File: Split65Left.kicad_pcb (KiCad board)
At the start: 2 copper layers, 176.6 x 97.8 mm, 77 parts, among them J1 Jack4, J2 OLED, SW1 SW_PUSH, SW10 SW_PUSH, SW11 SW_PUSH, SW12 SW_PUSH, SW13 SW_PUSH, SW14 SW_PUSH, SW15 SW_PUSH, SW16 SW_PUSH, SW17 SW_PUSH, SW18 SW_PUSH, SW19 SW_PUSH, SW2 SW_PUSH, SW20 SW_PUSH, SW21 SW_PUSH, SW22 SW_PUSH, SW23 SW_PUSH, SW24 SW_PUSH, SW25 SW_PUSH, SW26 SW_PUSH, SW27 SW_PUSH, SW28 SW_PUSH, SW29 SW_PUSH, SW3 SW_PUSH, SW30 SW_PUSH, SW31 SW_RST, SW4 SW_PUSH, SW5 SW_PUSH, SW6 SW_PUSH, SW7 SW_PUSH, SW8 SW_PUSH, SW9 SW_PUSH, U1 proton_c

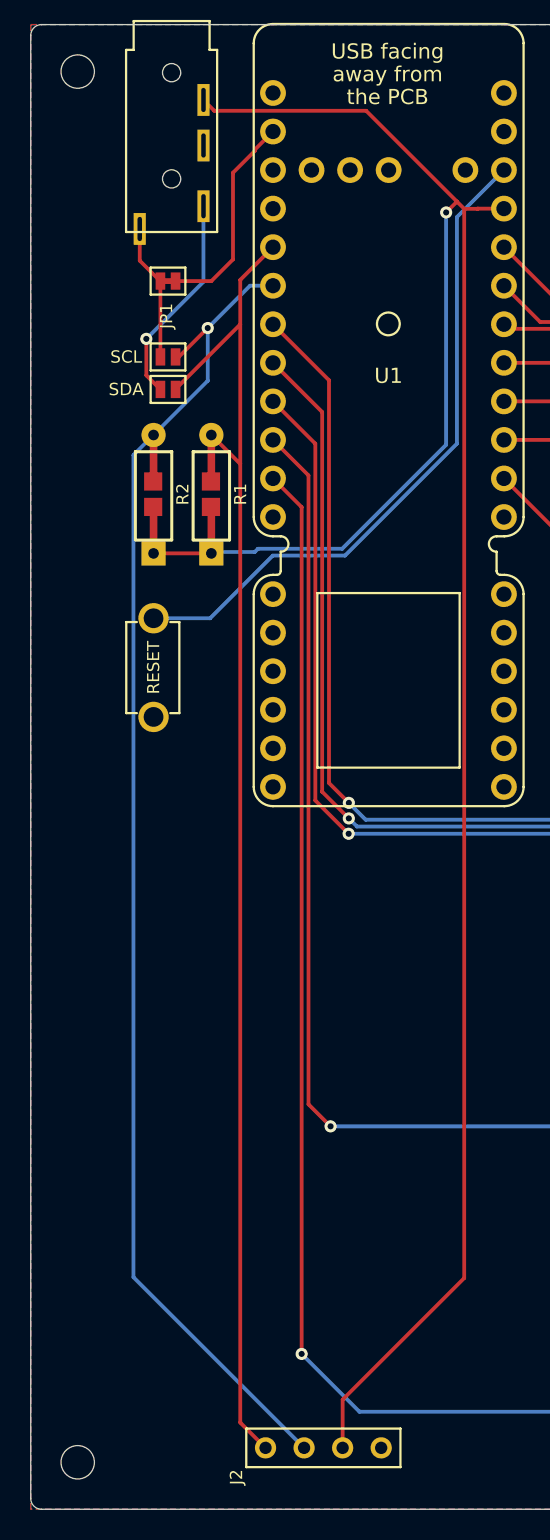
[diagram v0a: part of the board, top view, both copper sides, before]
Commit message: modified:   Split65Left-cache.lib 	modified:   Split65Left.kicad_pcb 	modified:   Split65Left.kicad_pcb-bak 	modified:   Split65Left.net 	modified:   Split65Left.sch 	modified:   Split65Left.sch-bak 	modified:   Split65Right-cache.lib 	modified:   Split65Right.kicad_pcb 	modified:   Split65Right.kicad_pcb-bak 	modified:   Split65Right.net 	modified:   Split65Right.sch 	modified:   Split65Right.sch-bak
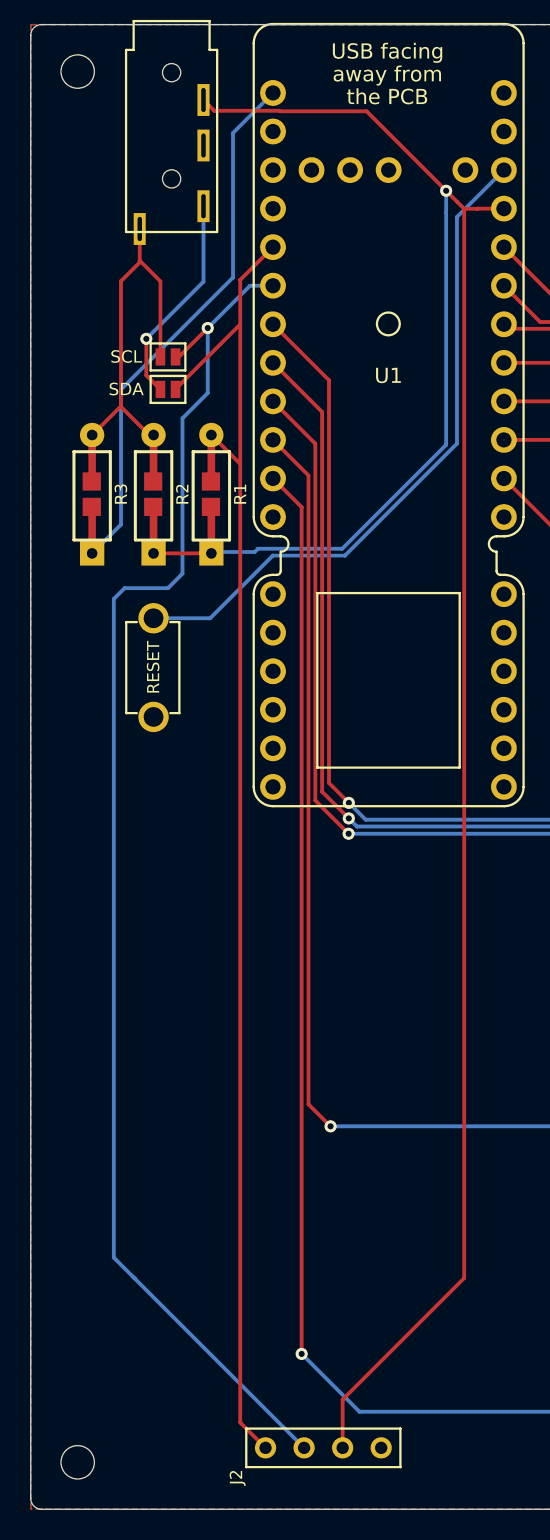
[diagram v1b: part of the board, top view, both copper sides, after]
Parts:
- removed JP1: Jumper, footprints:jumper_data
- added R3: 120, footprints:R_1608_axial, F.Cu at (62.6, 74.3)
- R1, R2: value R -> 5k
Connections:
- R2 pad 2: SCL -> Net-(J1-PadT)
- U1 pad A10: DATA -> Net-(U1-PadA10)
- U1 pad A9: LED -> DATA
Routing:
- net DATA: track 13.9 -> 38.3 mm
- net Net-(J1-PadT): track 8.99 -> 30.9 mm

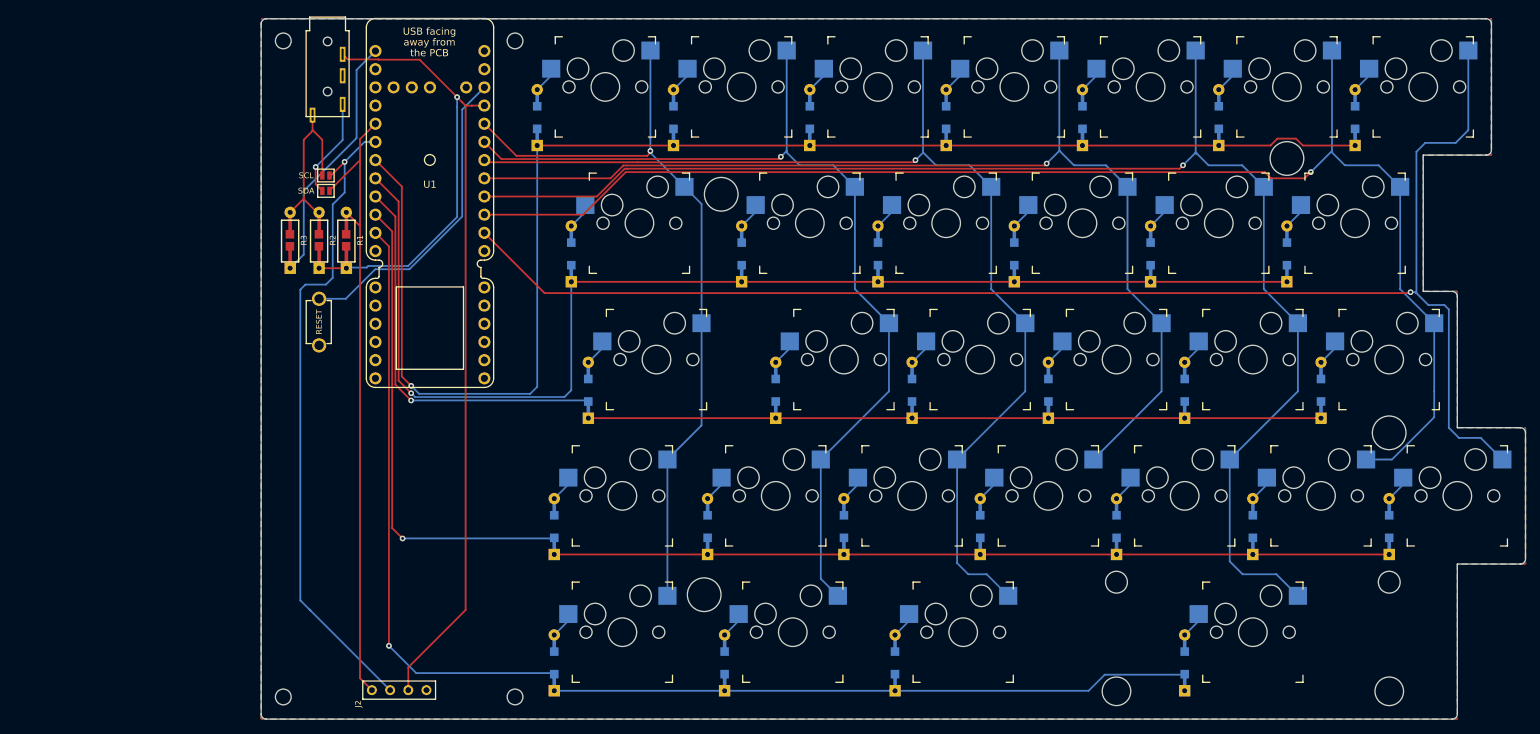
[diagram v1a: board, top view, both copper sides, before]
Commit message: Added Plates for left side
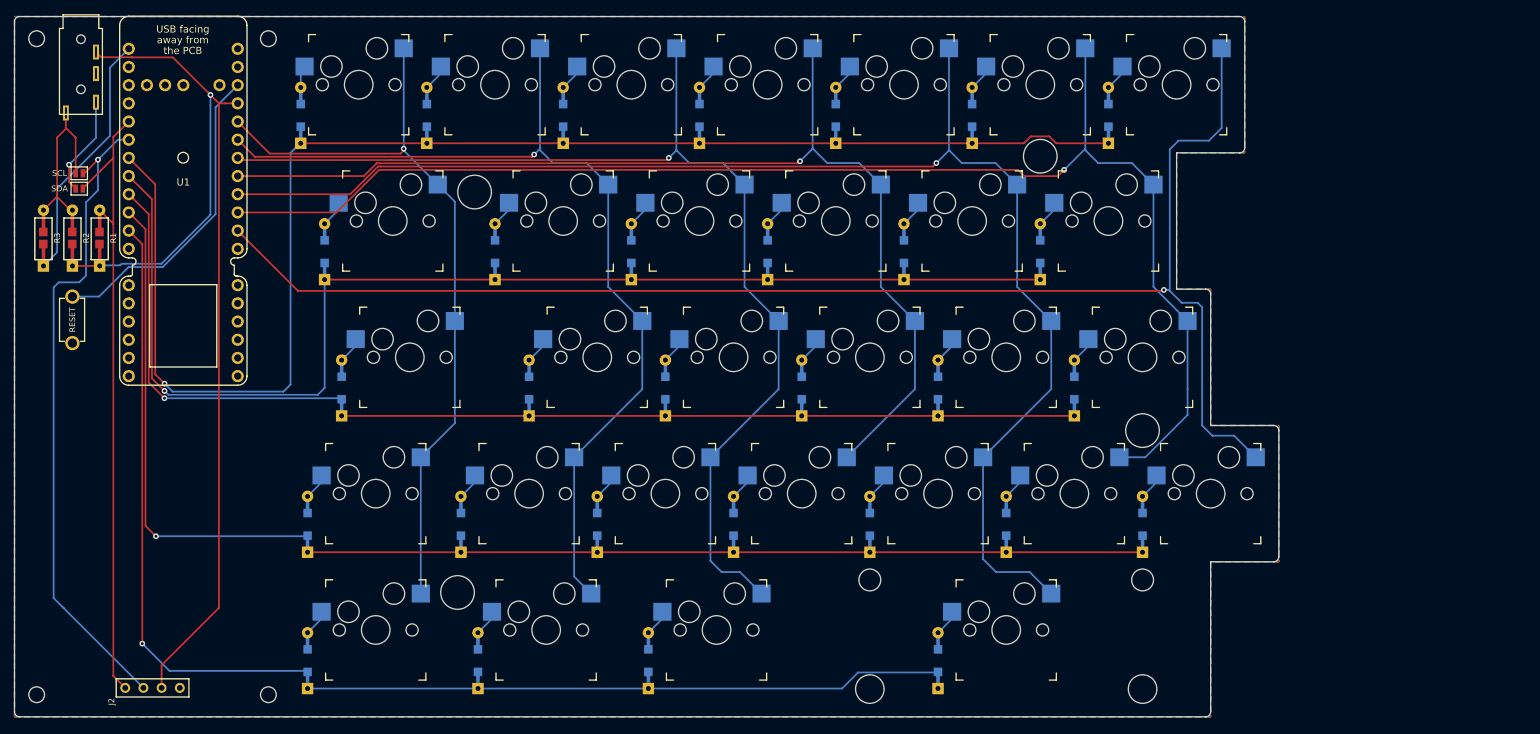
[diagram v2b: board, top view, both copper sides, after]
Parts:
- U1: value proton_c -> Proton_C
- moved D26 34.5 mm to (181.7, 113.9)
- moved HOLE_3M 34.5 mm to (181.7, 100.8)
- moved SW19 34.5 mm to (181.7, 90.6)
- moved D10 34.5 mm to (110.3, 75.8)
- moved D15 34.5 mm to (96.0, 94.9)
- moved D2 34.5 mm to (81.7, 56.8)
- moved D23 34.5 mm to (124.5, 113.9)
- moved D28 34.5 mm to (88.8, 133.0)
- moved HOLE_3M 34.5 mm to (88.4, 67.5)
- moved SW16 34.5 mm to (124.5, 90.6)
- moved SW21 34.5 mm to (96.0, 109.6)
- moved SW29 34.5 mm to (122.2, 128.7)
- moved SW3 34.5 mm to (110.3, 52.5)
- moved HOLE_M2 34.5 mm to (59.6, 137.7)
- moved HOLE_M2 34.5 mm to (59.6, 46.1)
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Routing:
- net row0: track 200.8 -> 200.0 mm

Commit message: Updated some small things - removed 3u buttons
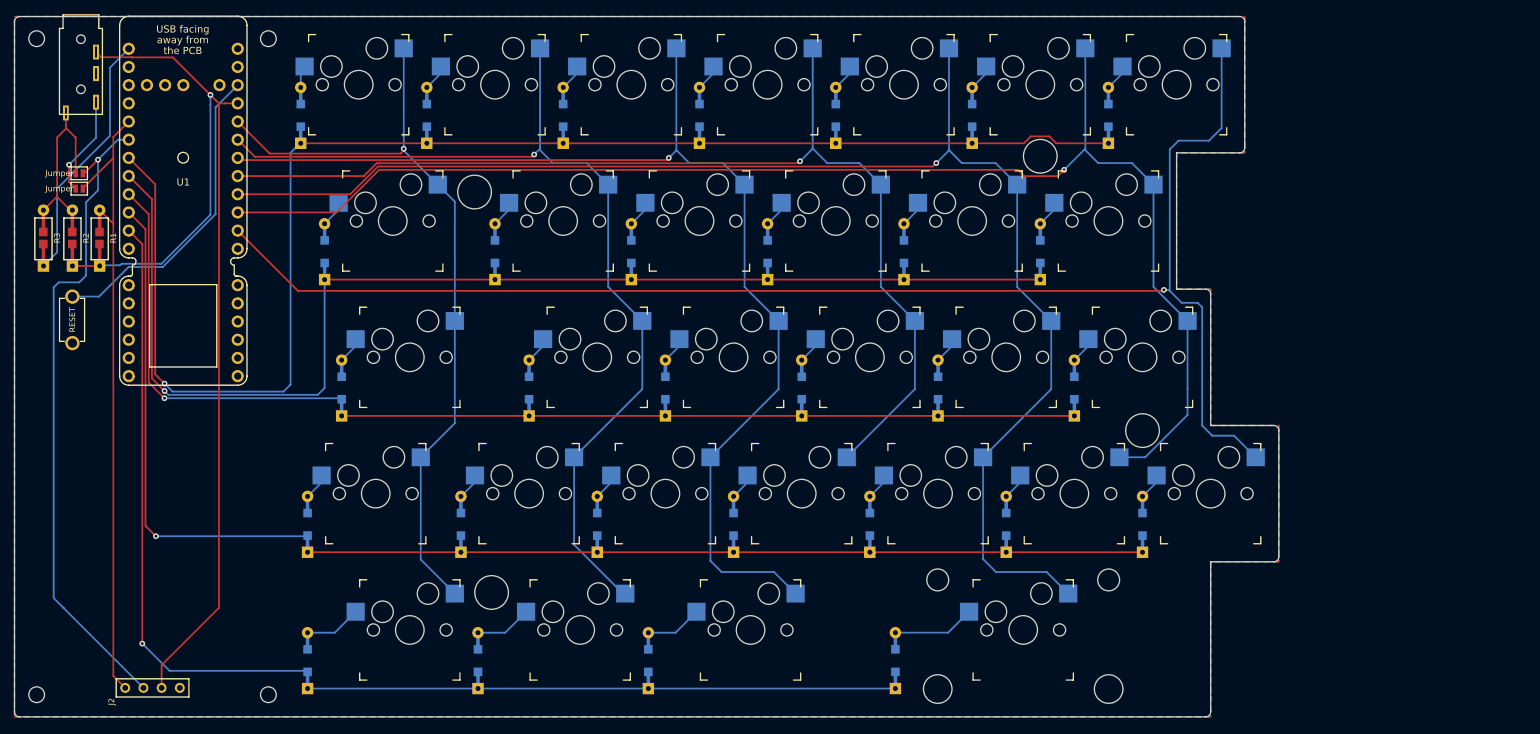
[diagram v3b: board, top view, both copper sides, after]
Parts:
- JP2: value SDA -> Jumper
- JP3: value SCL -> Jumper
- SW30: footprint footprints:KailhSocket-3U -> footprints:KailhSocket-2.75U
- U1: value Proton_C -> proton_c
- moved D30 5.96 mm to (147.1, 133.0)
- moved HOLE_3M 4.76 mm to (90.7, 123.4)
- moved SW27 4.76 mm to (79.3, 128.7)
- moved SW28 4.76 mm to (103.1, 128.7)
- moved SW29 4.75 mm to (126.9, 128.7)
- moved SW30 2.37 mm to (165.0, 128.7)
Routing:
- net Net-(D30-Pad2): track 3.74 -> 11.5 mm
- net row4: track 174.6 -> 167.7 mm
- net col2: track 155.2 -> 160.0 mm
- net Net-(D28-Pad2): track 3.74 -> 7.93 mm
- net Net-(D27-Pad2): track 3.74 -> 7.93 mm
- net Net-(D29-Pad2): track 3.74 -> 7.93 mm
- net col4: track 197.5 -> 199.8 mm
- net col1: track 133.4 -> 135.6 mm
- net col0: track 106.6 -> 108.5 mm
